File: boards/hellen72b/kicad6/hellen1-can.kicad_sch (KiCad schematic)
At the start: 6 parts

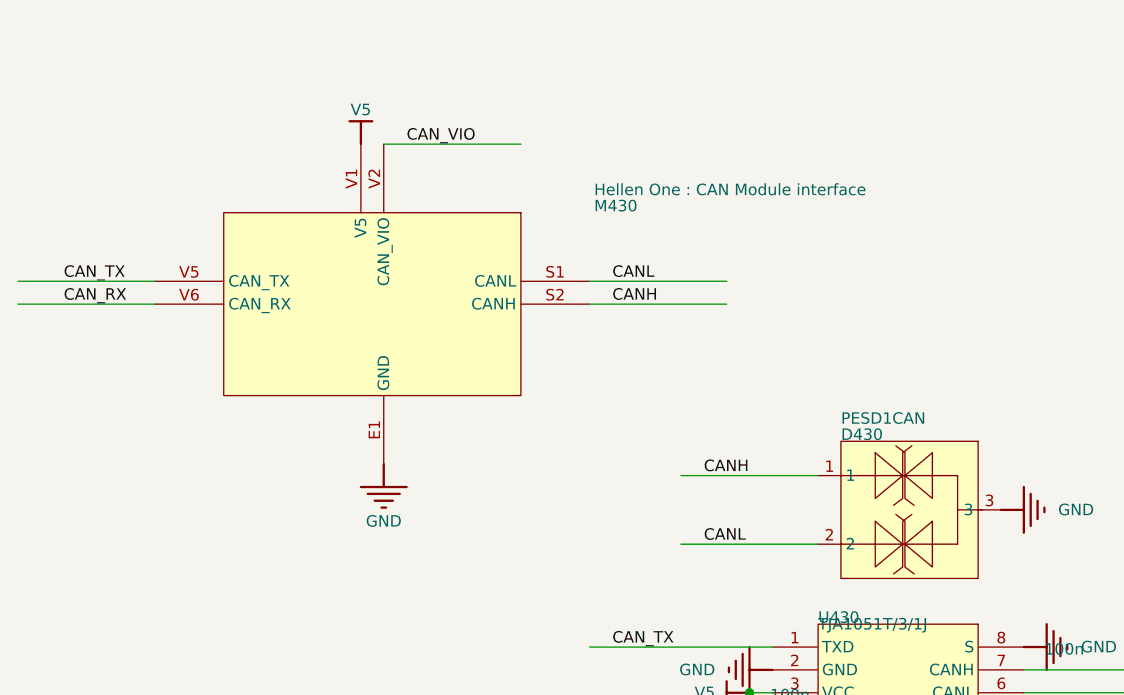
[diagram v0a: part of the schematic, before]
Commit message: update after refactoring can,lin,sd,stlink
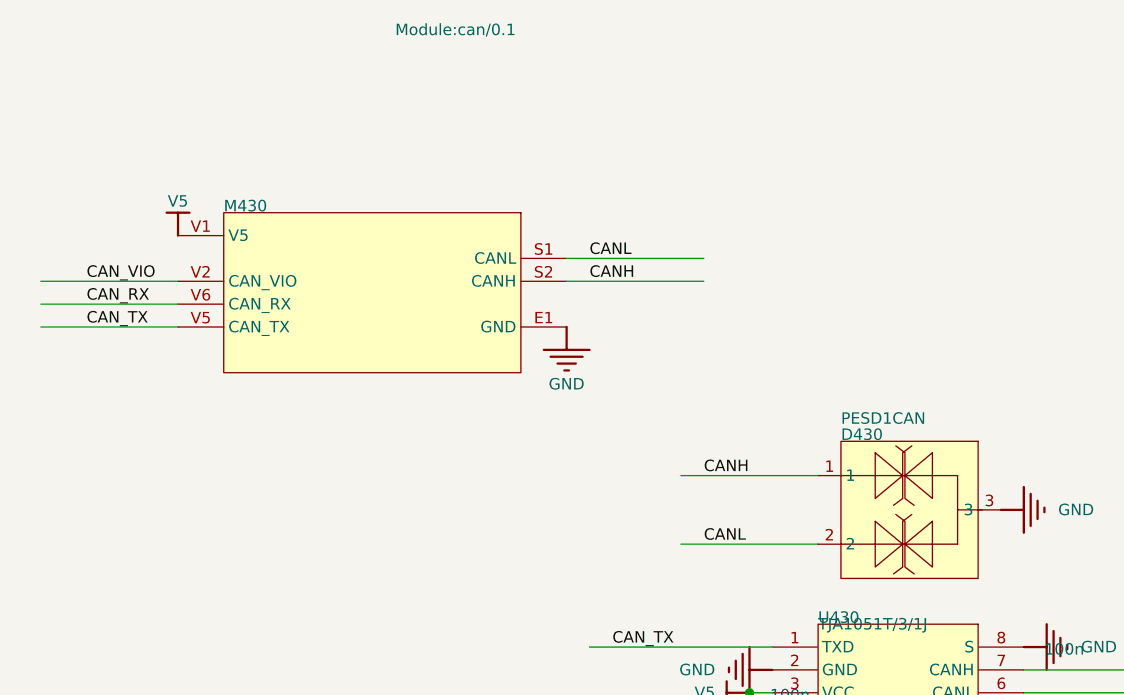
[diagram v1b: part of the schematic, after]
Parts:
- M430: Comment Hellen One : CAN Module interface -> Module:can/0.1
